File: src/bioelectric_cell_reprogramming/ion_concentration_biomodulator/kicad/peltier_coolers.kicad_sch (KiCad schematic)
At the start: 4 parts, among them J20 6620XX11122_66200211122, J7 6620XX11122_66200211122

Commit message: fix: ERC errors
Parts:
- J20, J7: footprint 1x02_socket_66200211122.pretty:66200211122 -> 6620XX11122_66200211122:66200211122
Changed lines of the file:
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@@
 			)
 		)
-		(property "Footprint" "1x02_socket_66200211122.pretty:66200211122"
+		(property "Footprint" "6620XX11122_66200211122:66200211122"
 			(at 144.78 102.87 0)
 			(effects
@@
 			)
 		)
-		(property "Footprint" "1x02_socket_66200211122.pretty:66200211122"
+		(property "Footprint" "6620XX11122_66200211122:66200211122"
 			(at 144.78 72.39 0)
 			(effects

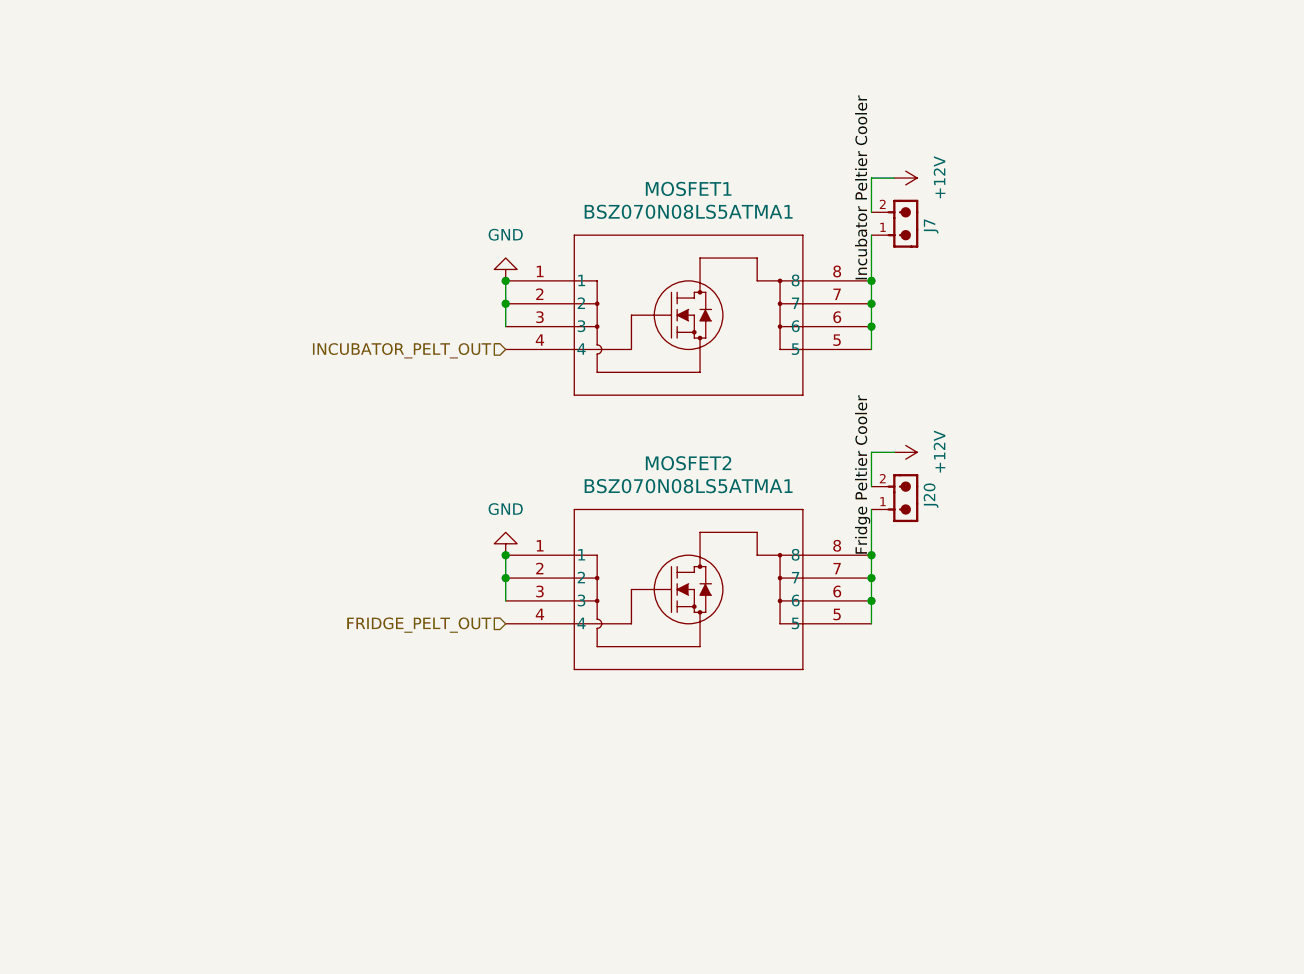
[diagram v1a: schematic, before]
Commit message: fix: replace fridge peltier cooler FET with an h-bridge
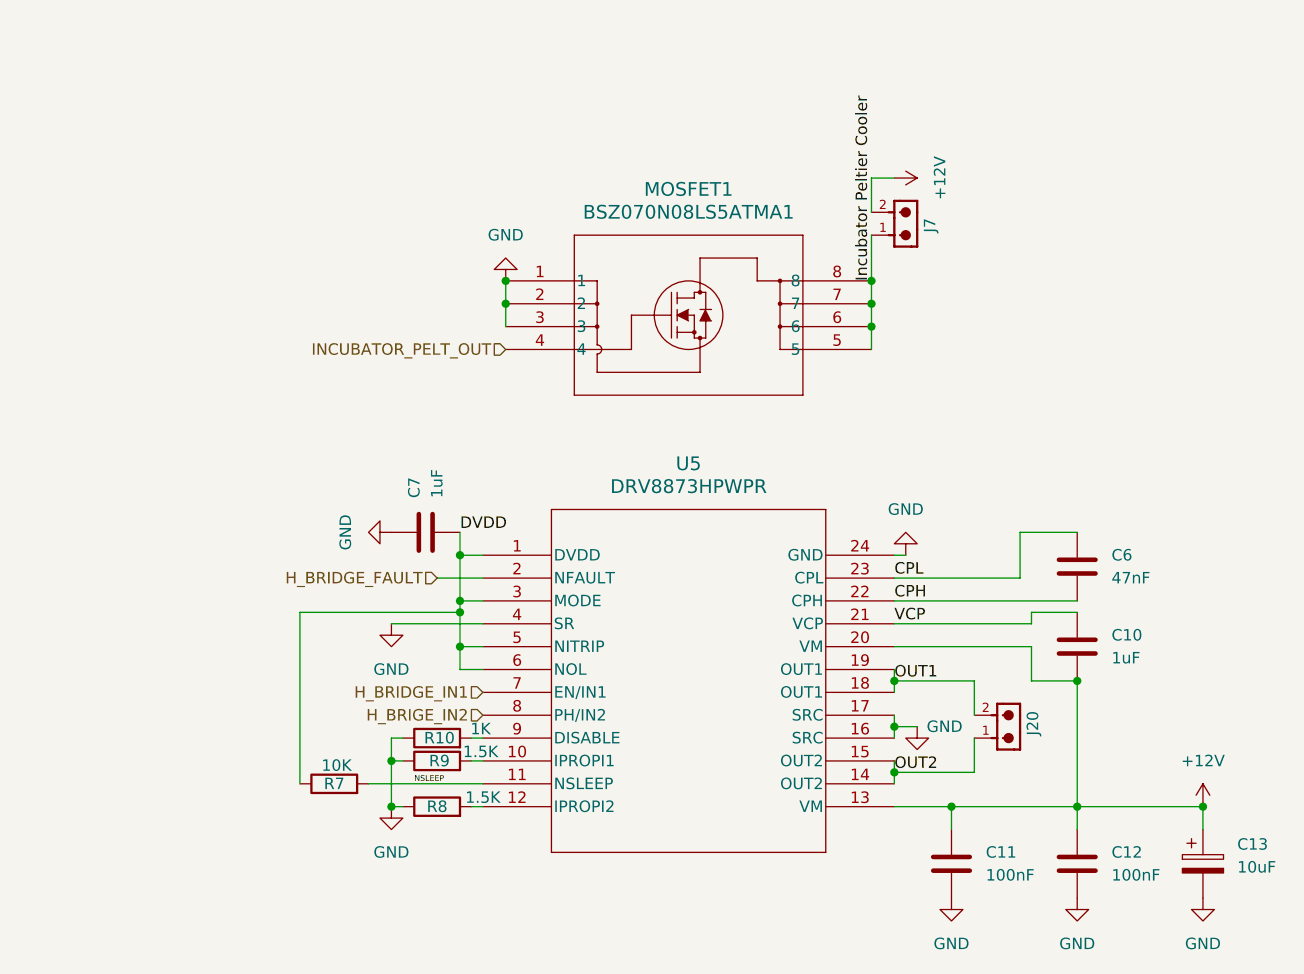
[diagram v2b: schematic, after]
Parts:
- removed MOSFET2: BSZ070N08LS5ATMA1, TSDSON-8-FL_INF, symbol BSZ070N08LS5ATMA1:BSZ070N08LS5ATMA1
- added C10: 1uF, Capacitor_SMD:C_0402_1005Metric, symbol Device:C
- added C11, C12: 100nF, Capacitor_SMD:C_0402_1005Metric, symbol Device:C
- added C13: 10uF, Capacitor_SMD:CP_Elec_3x5.3, symbol Device:C_Polarized
- added C6: 47nF, Capacitor_SMD:C_0402_1005Metric, symbol Device:C
- added C7: 1uF, Capacitor_SMD:C_0201_0603Metric, symbol Device:C
- added R10: 1K, Resistor_SMD:R_0201_0603Metric, symbol Device:R
- added R7: 10K, Resistor_SMD:R_0201_0603Metric, symbol Device:R
- added R8, R9: 1.5K, Resistor_SMD:R_0201_0603Metric, symbol Device:R
- added U5: DRV8873HPWPR, DRV8873HPWPR.pretty:PWP24_TEX, symbol DRV8873HPWPR:DRV8873HPWPR
- J20, J7: footprint 6620XX11122_66200211122:66200211122 -> 1x02_socket_66200211122.pretty:66200211122
- MOSFET1: footprint TSDSON-8-FL_INF -> BSZ070N08LS5ATMA1:TSDSON-8-FL_INF
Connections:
- net +12V: now also C10.2, C11.1, C12.1, C13.1, U5.13 (VM), U5.20 (VM); no longer J20.2
- net GND: now also C11.2, C12.2, C13.2, C7.1, R10.1, R8.1, R9.1, U5.16 (SRC), U5.17 (SRC), U5.24 (GND), U5.4 (SR)
- net Fridge Peltier Cooler renamed OUT2
- net OUT2: now also U5.14 (OUT2), U5.15 (OUT2)
- new net: R10.2, U5.9 (DISABLE)
- new net: R8.2, U5.12 (IPROPI2)
- new net: R9.2, U5.10 (IPROPI1)
- new net CPH: C6.2, U5.22 (CPH)
- new net CPL: C6.1, U5.23 (CPL)
- new net DVDD: C7.2, R7.1, U5.1 (DVDD), U5.3 (MODE), U5.5 (NITRIP), U5.6 (NOL)
- new net H_BRIDGE_FAULT: U5.2 (NFAULT)
- new net H_BRIDGE_IN1: U5.7 (EN/IN1)
- new net H_BRIGE_IN2: U5.8 (PH/IN2)
- new net NSLEEP: R7.2, U5.11 (NSLEEP)
- new net OUT1: J20.2, U5.18 (OUT1), U5.19 (OUT1)
- new net VCP: C10.1, U5.21 (VCP)

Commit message: fix: new co2 sensor
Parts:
- J20, J7: footprint 1x02_socket_66200211122.pretty:66200211122 -> 6620XX11122_66200211122:66200211122
- MOSFET1: footprint BSZ070N08LS5ATMA1:TSDSON-8-FL_INF -> TSDSON-8-FL_INF
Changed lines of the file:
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@@
 			)
 		)
-		(property "Footprint" "1x02_socket_66200211122.pretty:66200211122"
+		(property "Footprint" "6620XX11122_66200211122:66200211122"
 			(at 156.21 128.27 0)
 			(effects
@@
 			)
 		)
-		(property "Footprint" "BSZ070N08LS5ATMA1:TSDSON-8-FL_INF"
+		(property "Footprint" "TSDSON-8-FL_INF"
 			(at 99.06 77.47 0)
 			(effects
@@
 			)
 		)
-		(property "Footprint" "1x02_socket_66200211122.pretty:66200211122"
+		(property "Footprint" "6620XX11122_66200211122:66200211122"
 			(at 144.78 72.39 0)
 			(effects

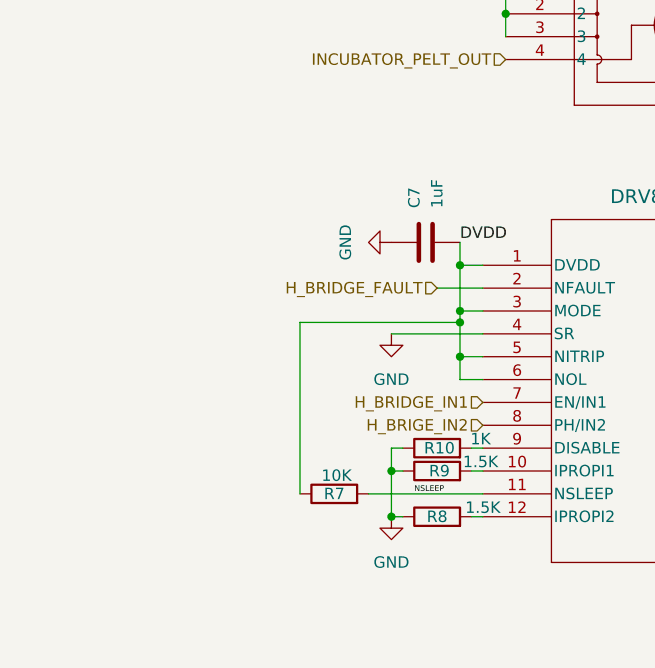
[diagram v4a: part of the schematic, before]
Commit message: fix: DRV8873 nSLEEP and nFAULT pull-ups
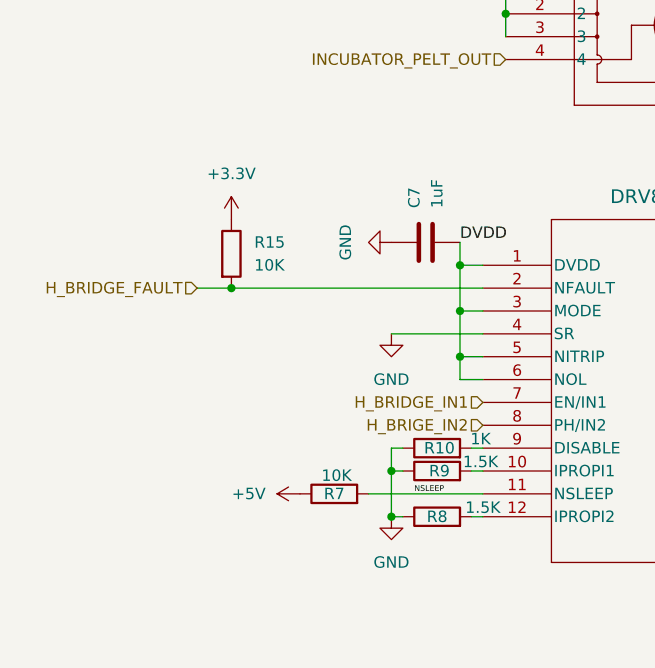
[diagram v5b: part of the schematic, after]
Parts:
- added R15: 10K, Resistor_SMD:R_0201_0603Metric, symbol Device:R
- J20, J7: footprint 6620XX11122_66200211122:66200211122 -> 1x02_socket_66200211122.pretty:66200211122
- MOSFET1: footprint TSDSON-8-FL_INF -> BSZ070N08LS5ATMA1:TSDSON-8-FL_INF
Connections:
- net DVDD: no longer R7.1
- net H_BRIDGE_FAULT: now also R15.2
- new net +3.3V: R15.1
- new net +5V: R7.1
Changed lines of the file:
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@@
 	(paper "A4")
+	(junction
+		(at 68.58 110.49)
+		(diameter 0)
+		(color 0 0 0 0)
+	)
 	(junction
 		(at 86.36 135.89)
@@
 	)
 	(junction
-		(at 93.98 114.3)
-		(diameter 0)
-		(color 0 0 0 0)
-	)
-	(junction
 		(at 93.98 107.95)
 		(diameter 0)
@@
 	(wire
 		(pts
-			(xy 76.2 114.3) (xy 93.98 114.3)
-		)
-		(stroke
-			(width 0)
-			(type default)
-		)
-	)
-	(wire
-		(pts
 			(xy 176.53 138.43) (xy 176.53 135.89)
 		)
@@
 	(wire
 		(pts
+			(xy 64.77 110.49) (xy 68.58 110.49)
+		)
+		(stroke
+			(width 0)
+			(type default)
+		)
+	)
+	(wire
+		(pts
 			(xy 142.24 127) (xy 142.24 128.27)
 		)
@@
 	(wire
 		(pts
-			(xy 93.98 114.3) (xy 93.98 113.03)
+			(xy 93.98 113.03) (xy 93.98 118.11)
 		)
 		(stroke
@@
 	(wire
 		(pts
-			(xy 96.52 110.49) (xy 91.44 110.49)
-		)
-		(stroke
-			(width 0)
-			(type default)
-		)
-	)
-	(wire
-		(pts
 			(xy 142.24 130.81) (xy 142.24 132.08)
 		)
@@
 	(wire
 		(pts
-			(xy 76.2 114.3) (xy 76.2 133.35)
-		)
-		(stroke
-			(width 0)
-			(type default)
-		)
-	)
-	(wire
-		(pts
 			(xy 148.59 135.89) (xy 162.56 135.89)
 		)
@@
 	(wire
 		(pts
+			(xy 68.58 110.49) (xy 96.52 110.49)
+		)
+		(stroke
+			(width 0)
+			(type default)
+		)
+	)
+	(wire
+		(pts
 			(xy 86.36 130.81) (xy 86.36 135.89)
 		)
@@
 		(pts
 			(xy 162.56 138.43) (xy 162.56 135.89)
-		)
-		(stroke
-			(width 0)
-			(type default)
-		)
-	)
-	(wire
-		(pts
-			(xy 93.98 118.11) (xy 93.98 114.3)
 		)
 		(stroke
@@
 	(hierarchical_label "H_BRIDGE_FAULT"
 		(shape input)
-		(at 91.44 110.49 180)
+		(at 64.77 110.49 180)
 		(fields_autoplaced yes)
 		(effects
@@
 			)
 		)
-		(property "Footprint" "6620XX11122_66200211122:66200211122"
+		(property "Footprint" "1x02_socket_66200211122.pretty:66200211122"
 			(at 156.21 128.27 0)
 			(effects
@@
 			)
 		)
-		(property "Footprint" "TSDSON-8-FL_INF"
+		(property "Footprint" "BSZ070N08LS5ATMA1:TSDSON-8-FL_INF"
 			(at 99.06 77.47 0)
 			(effects
@@
 	)
 	(symbol
+		(lib_id "power:+3.3V")
+		(at 68.58 102.87 0)
+		(unit 1)
+		(exclude_from_sim no)
+		(in_bom yes)
+		(on_board yes)
+		(dnp no)
+		(fields_autoplaced yes)
+		(property "Reference" "#PWR066"
+			(at 68.58 106.68 0)
+			(effects
+				(font
+					(size 1.27 1.27)
+				)
+				(hide yes)
+			)
+		)
+		(property "Value" "+3.3V"
+			(at 68.58 97.79 0)
+			(effects
+				(font
+					(size 1.27 1.27)
+				)
+			)
+		)
+		(property "Footprint" ""
+			(at 68.58 102.87 0)
+			(effects
+				(font
+					(size 1.27 1.27)
+				)
+				(hide yes)
+			)
+		)
+		(property "Datasheet" ""
+			(at 68.58 102.87 0)
+			(effects
+				(font
+					(size 1.27 1.27)
+				)
+				(hide yes)
+			)
+		)
+		(property "Description" "Power symbol creates a global label with name \"+3.3V\""
+			(at 68.58 102.87 0)
+			(effects
+				(font
+					(size 1.27 1.27)
+				)
+				(hide yes)
+			)
+		)
+		(pin "1"
+		)
+		(instances
+			(project ""
+				(path "/bae20e05-e1d7-4036-8683-639bb0f1fbc7/d00a1c36-08f1-42bb-994d-12073bc9bf7e"
+					(reference "#PWR066")
+					(unit 1)
+				)
+			)
+		)
+	)
+	(symbol
 		(lib_id "power:GND")
 		(at 148.59 146.05 0)
@@
 	)
 	(symbol
+		(lib_id "Device:R")
+		(at 68.58 106.68 0)
+		(unit 1)
+		(exclude_from_sim no)
+		(in_bom yes)
+		(on_board yes)
+		(dnp no)
+		(fields_autoplaced yes)
+		(property "Reference" "R15"
+			(at 71.12 105.4099 0)
+			(effects
+				(font
+					(size 1.27 1.27)
+				)
+				(justify left)
+			)
+		)
+		(property "Value" "10K"
+			(at 71.12 107.9499 0)
+			(effects
+				(font
+					(size 1.27 1.27)
+				)
+				(justify left)
+			)
+		)
+		(property "Footprint" "Resistor_SMD:R_0201_0603Metric"
+			(at 66.802 106.68 90)
+			(effects
+				(font
+					(size 1.27 1.27)
+				)
+				(hide yes)
+			)
+		)
+		(property "Datasheet" "~"
+			(at 68.58 106.68 0)
+			(effects
+				(font
+					(size 1.27 1.27)
+				)
+				(hide yes)
+			)
+		)
+		(property "Description" "Resistor"
+			(at 68.58 106.68 0)
+			(effects
+				(font
+					(size 1.27 1.27)
+				)
+				(hide yes)
+			)
+		)
+		(pin "1"
+		)
+		(pin "2"
+		)
+		(instances
+			(project ""
+				(path "/bae20e05-e1d7-4036-8683-639bb0f1fbc7/d00a1c36-08f1-42bb-994d-12073bc9bf7e"
+					(reference "R15")
+					(unit 1)
+				)
+			)
+		)
+	)
+	(symbol
 		(lib_id "6620XX11122_66200211122:6620XX11122_66200211122")
 		(at 144.78 72.39 270)
@@
 			)
 		)
-		(property "Footprint" "6620XX11122_66200211122:66200211122"
+		(property "Footprint" "1x02_socket_66200211122.pretty:66200211122"
 			(at 144.78 72.39 0)
 			(effects
@@
 					(unit 1)
 				)
+			)
+		)
+	)
+	(symbol
+		(lib_id "power:+5V")
+		(at 76.2 133.35 90)
+		(unit 1)
+		(exclude_from_sim no)
+		(in_bom yes)
+		(on_board yes)
+		(dnp no)
+		(fields_autoplaced yes)
+		(property "Reference" "#PWR067"
+			(at 80.01 133.35 0)
+			(effects
+				(font
+					(size 1.27 1.27)
+				)
+				(hide yes)
+			)
+		)
+		(property "Value" "+5V"
+			(at 72.39 133.3499 90)
+			(effects
+				(font
+					(size 1.27 1.27)
+				)
+				(justify left)
+			)
+		)
+		(property "Footprint" ""
+			(at 76.2 133.35 0)
+			(effects
+				(font
+					(size 1.27 1.27)
+				)
+				(hide yes)
+			)
+		)
+		(property "Datasheet" ""
+			(at 76.2 133.35 0)
+			(effects
+				(font
+					(size 1.27 1.27)
+				)
+				(hide yes)
+			)
+		)
+		(property "Description" "Power symbol creates a global label with name \"+5V\""
+			(at 76.2 133.35 0)
+			(effects
+				(font
+					(size 1.27 1.27)
+				)
+				(hide yes)
+			)
+		)
+		(pin "1"
+		)
+		(instances
+			(project ""
+				(path "/bae20e05-e1d7-4036-8683-639bb0f1fbc7/d00a1c36-08f1-42bb-994d-12073bc9bf7e"
+					(reference "#PWR067")
+					(unit 1)
+				)
